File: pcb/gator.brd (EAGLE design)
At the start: 101.6 x 81.3 mm, 89 parts, among them J2 POWER_JACKPTH, X1 USB-A-S, Y1 12MHz

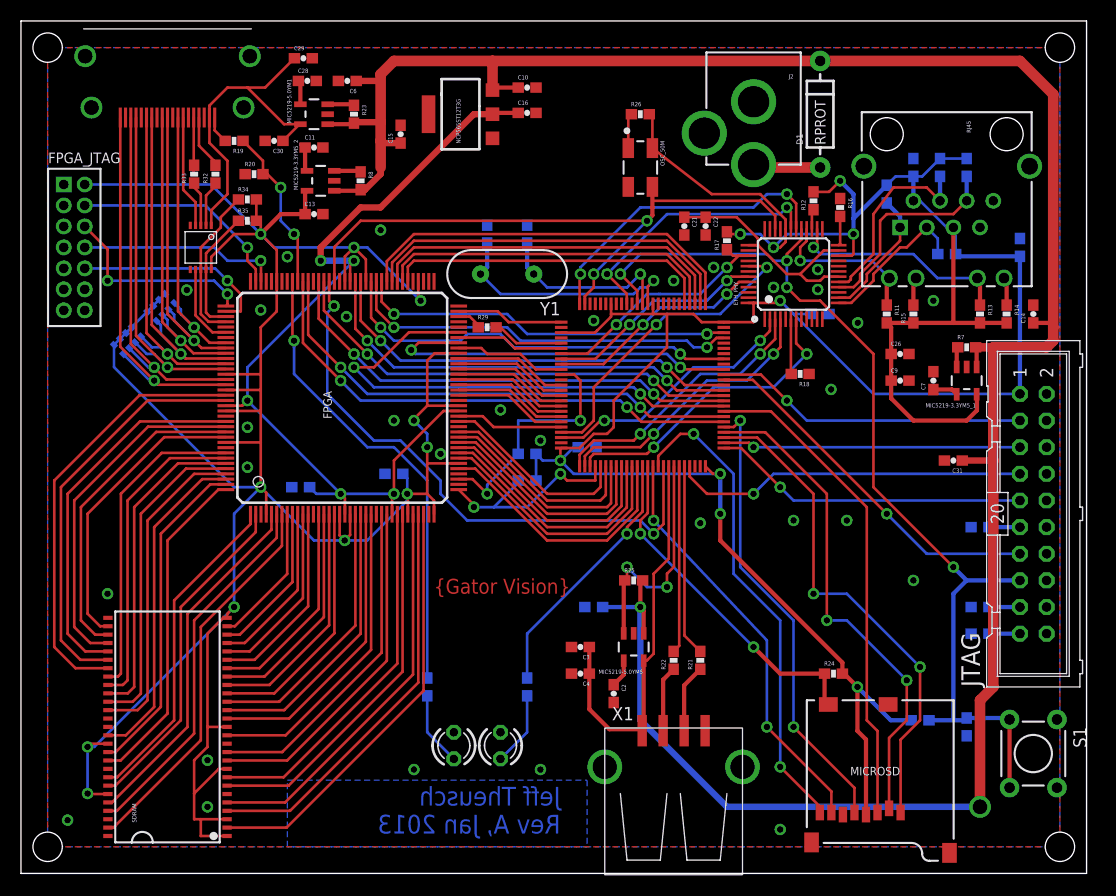
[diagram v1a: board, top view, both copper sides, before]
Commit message: Added tons of decoupling capacitors
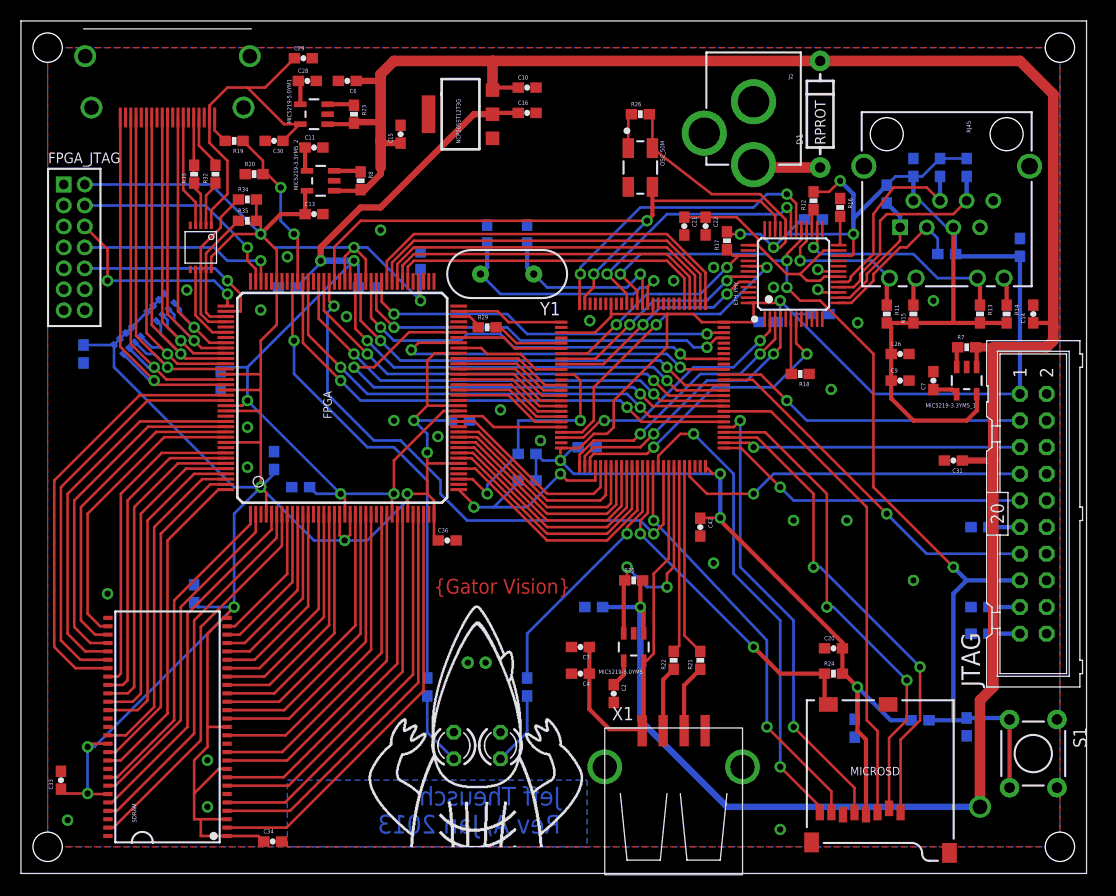
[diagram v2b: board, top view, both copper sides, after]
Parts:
- added C20: 10u, SparkFun-Passives:0603-CAP
- added C23, C32, C33, C34, C35, C36, C37, C38, C39, C40, C41, C42, C43, C44: 100n, SparkFun-Passives:0603-CAP
- added U$4: GATOR_HEAD, gator:GATOR_HEAD
- C13, C16, C30, C4, C9: value 2.2u -> 10u
- moved C12 11.5 mm to (24.1, 39.4), turned to 90 degrees
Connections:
- net +3V3: now also C20.2, C41.1, C42.1, C43.1, C44.1
- net GND: now also C20.1, C23.2, C32.2, C33.2, C34.2, C35.2, C36.2, C37.2, C38.2, C39.2, C40.2, C41.2, C42.2, C43.2, C44.2, U$4.L, U$4.R
- net VCCINT: now also C23.1, C32.1, C40.1
- net VCCIO: now also C33.1, C34.1, C35.1, C36.1, C37.1, C38.1, C39.1
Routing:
- net VCCIO: track 263.3 -> 286.0 mm
- net +3V3: track 272.8 -> 282.3 mm
- net VCCINT: track 86.8 -> 95.8 mm
- net GND: track 0.00 -> 4.17 mm, vias 31 -> 29
- net SD_D2: track 48.0 -> 46.5 mm
- net SD_D3: track 47.2 -> 46.5 mm
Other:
- board outline removed

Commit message: Added Fusion DRC and CAM settings; added SD SCLK pulldown; added large power supply caps
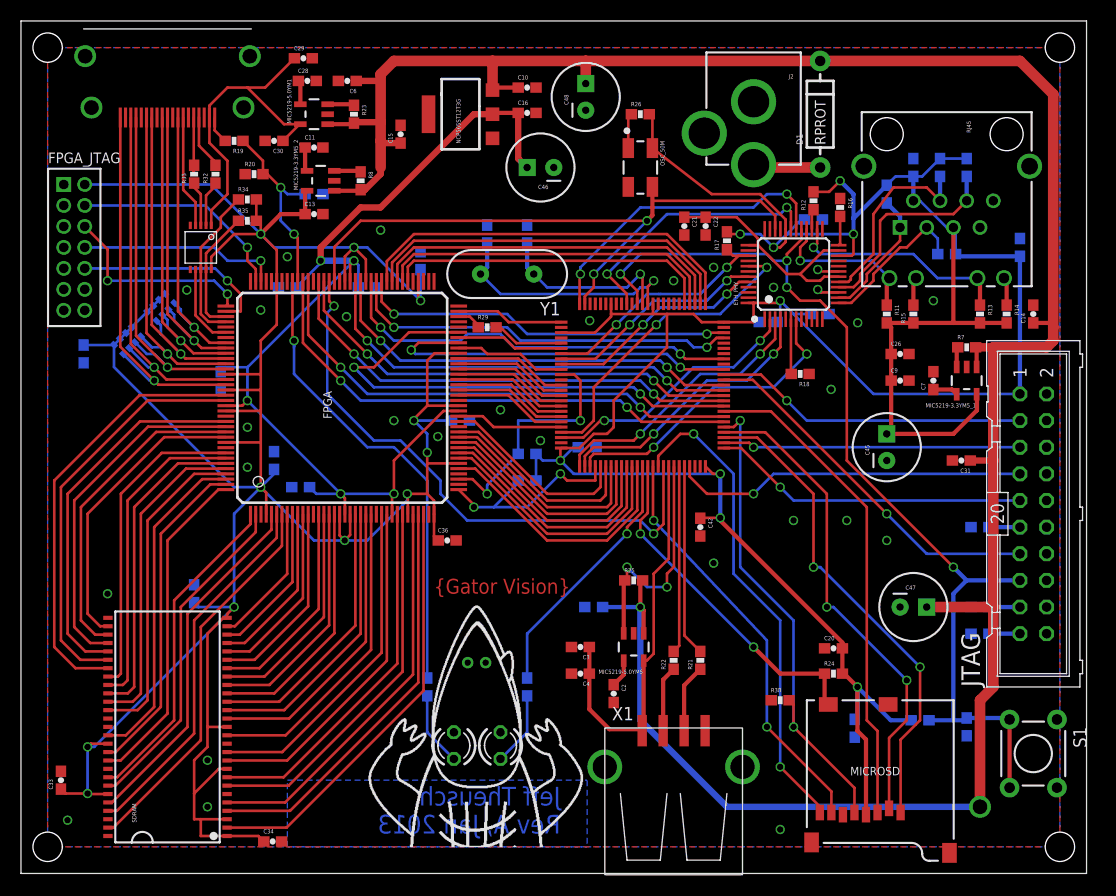
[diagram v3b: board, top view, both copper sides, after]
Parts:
- added C45, C46, C47, C48: 100u, SparkFun-Passives:CPOL-RADIAL-100UF-25V
- added C49: 100n, SparkFun-Passives:0603-CAP
- added R38: 10K, SparkFun-Passives:0603-RES
- C6: value 2.2u -> 10u
- R14, R15: value 110 -> 120
- R19: value 5K6 -> 4K7
- R20: value 10K -> 4K7
- R29: value 50 -> 51
- moved C31 0.76 mm to (89.7, 39.4)
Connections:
- net +3V3: now also C45.1
- net GND: now also C45.2, C46.2, C47.2, C48.2, C49.2, R38.1
- net HDMI_DETECT: now also C49.1
- net SD_CLK: now also R38.2
- net V+: now also C47.1, C48.1
- net VCCINT: now also C46.1
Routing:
- net V+: track 233.9 -> 241.7 mm
- net VCCINT: track 95.8 -> 101.3 mm
- net +3V3: track 282.3 -> 285.9 mm
- net SD_CLK: track 43.7 -> 46.4 mm
- net HDMI_DETECT: track 15.8 -> 18.4 mm

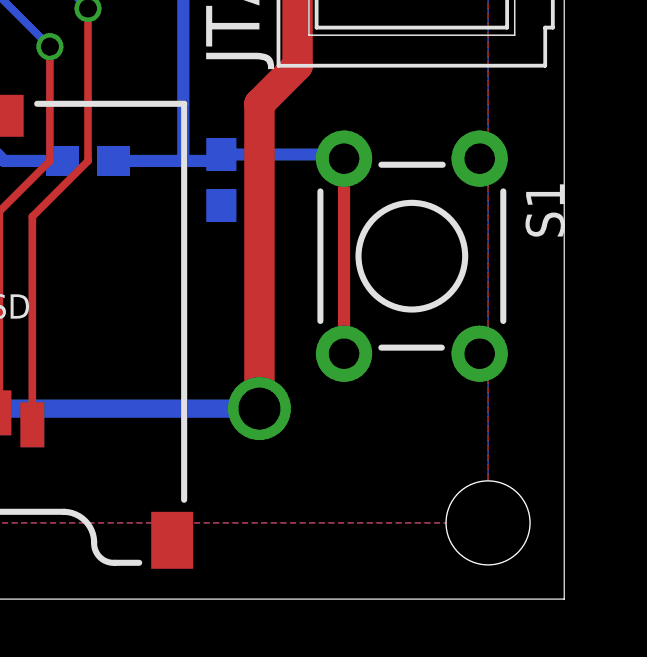
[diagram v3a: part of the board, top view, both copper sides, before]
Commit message: Renamed some parts for clarity
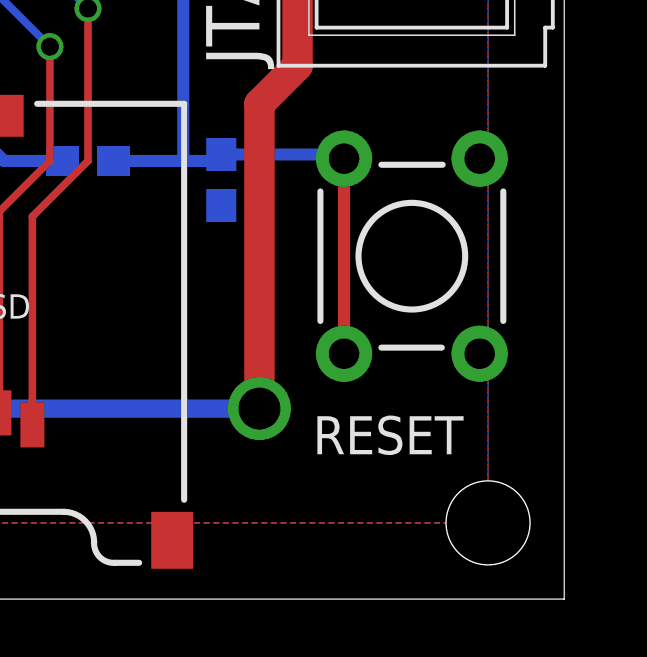
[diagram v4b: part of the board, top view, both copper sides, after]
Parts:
- renumbered S1 to RESET, U$1 to MCU

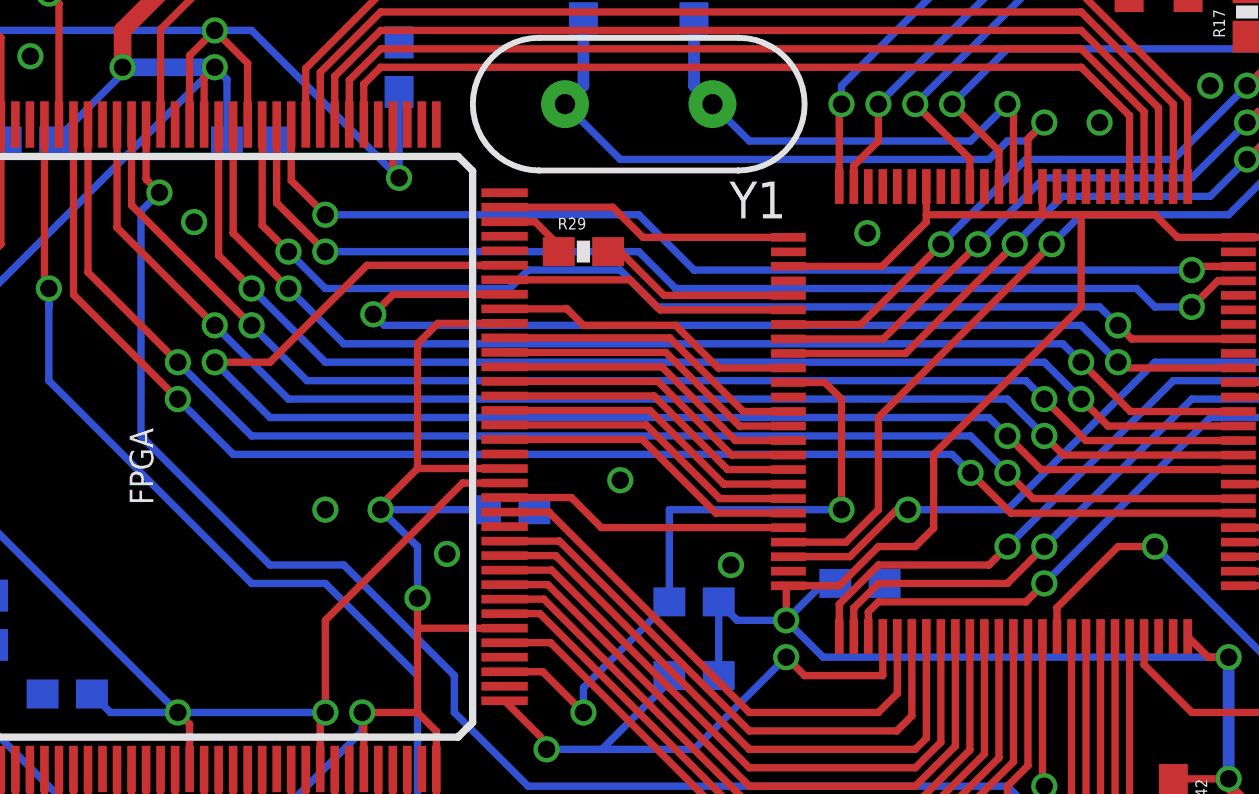
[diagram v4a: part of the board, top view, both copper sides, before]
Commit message: Moved FSMC_CLK to a clock input on the FPGA
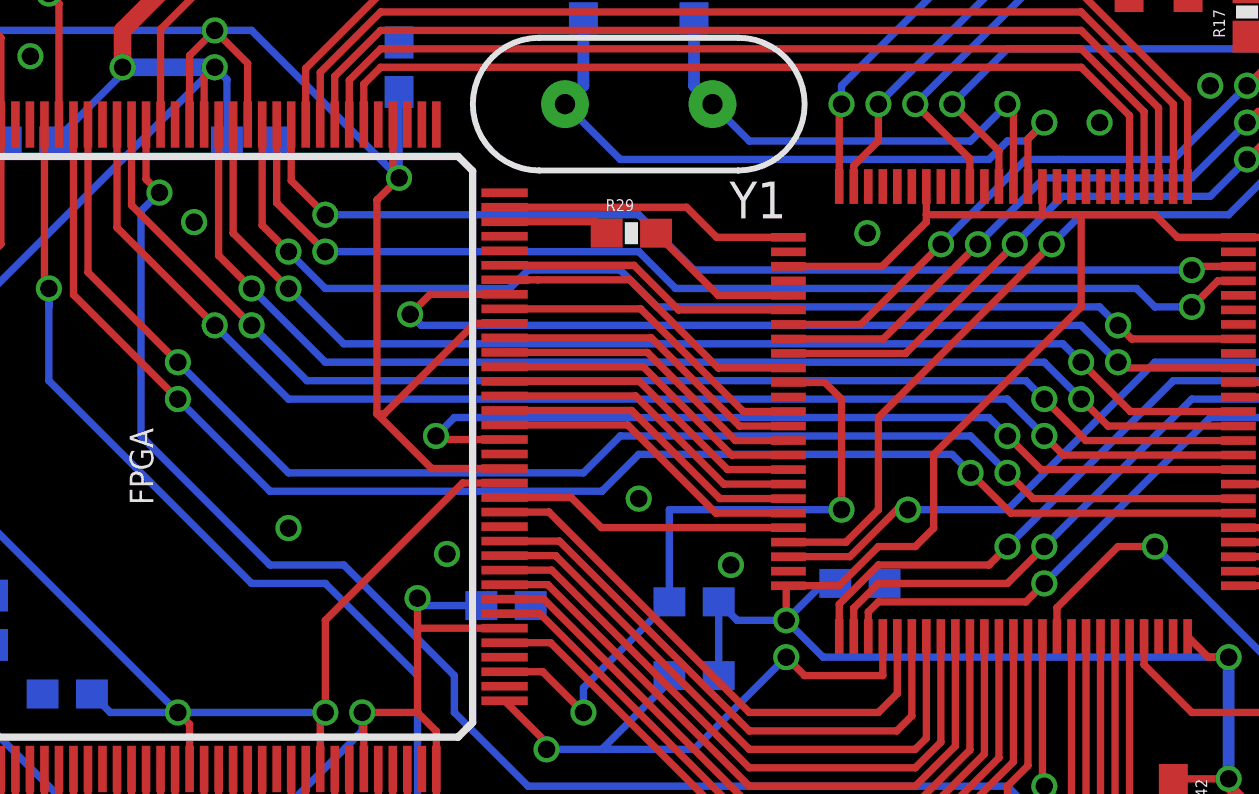
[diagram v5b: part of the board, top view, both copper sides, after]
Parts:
- moved C38 3.30 mm to (41.8, 39.9)
- moved R29 1.77 mm to (46.1, 52.7)
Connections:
- net D10: now also FPGA.P57; no longer FPGA.P56
- net D11: now also FPGA.P56; no longer FPGA.P55
- net D4: now also FPGA.P64; no longer FPGA.P62
- net D5: now also FPGA.P62; no longer FPGA.P61
- net D6: now also FPGA.P61; no longer FPGA.P60
- net D7: now also FPGA.P60; no longer FPGA.P59
- net D8: now also FPGA.P59; no longer FPGA.P58
- net D9: now also FPGA.P58; no longer FPGA.P57
- net FSMC_CLK: now also FPGA.P55; no longer FPGA.P67
- net SPI_MISO: now also FPGA.P67; no longer FPGA.P66
- net VSYNC: now also FPGA.P66; no longer FPGA.P64
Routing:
- net FSMC_CLK: track 48.2 -> 31.1 mm
- net CFG_DIN: track 35.4 -> 32.8 mm
- net VCCIO: track 286.0 -> 287.9 mm, vias 11 -> 10
- net CFG_CLK: track 6.84 -> 5.45 mm
- net N$33: track 2.42 -> 3.68 mm
- net D2: track 49.1 -> 50.2 mm
- net D3: track 47.9 -> 49.0 mm

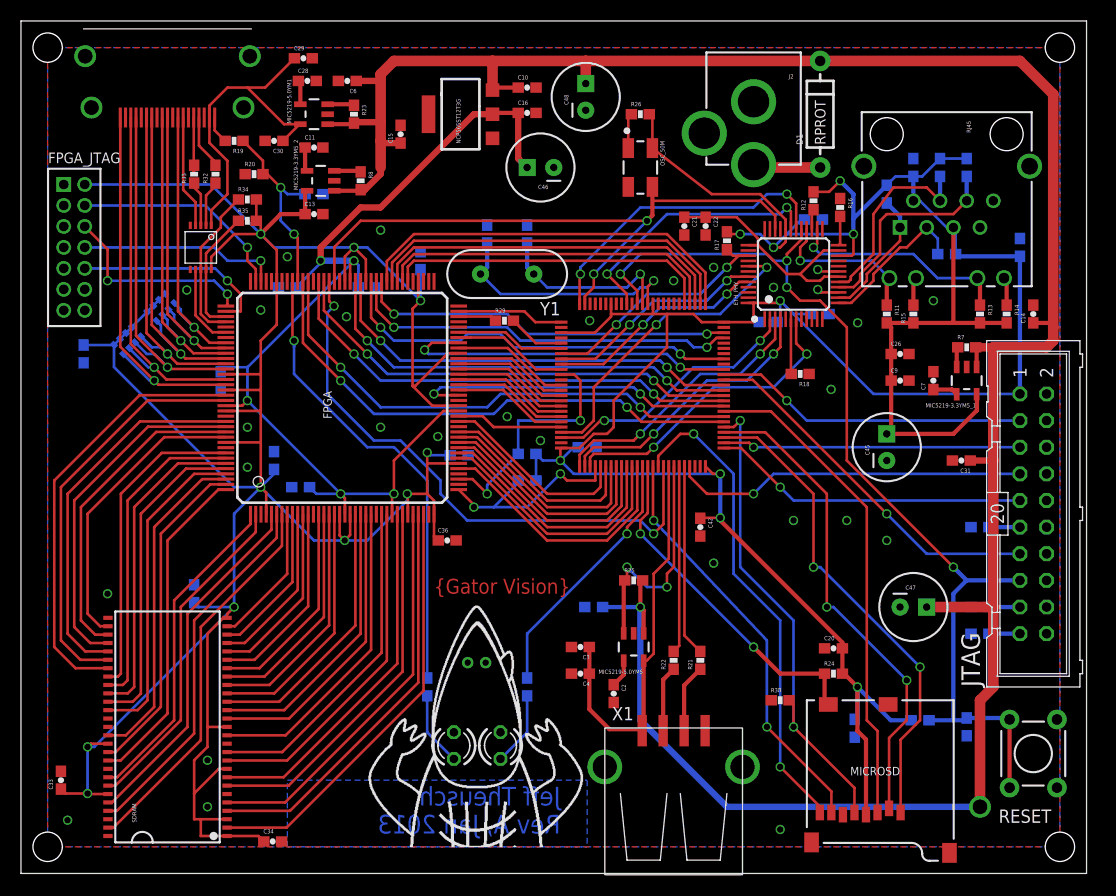
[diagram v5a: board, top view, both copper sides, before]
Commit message: Added pull-ups for sd card and ethernet
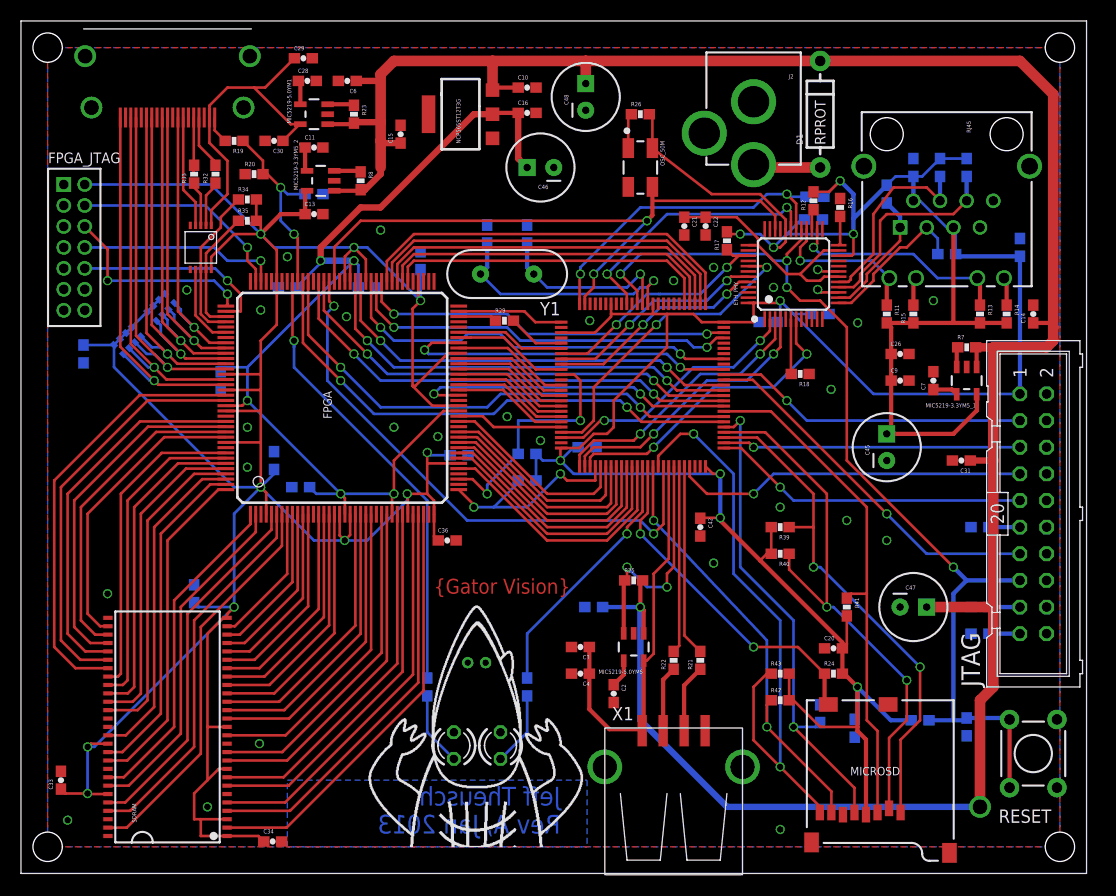
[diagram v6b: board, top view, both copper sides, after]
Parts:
- added R39, R40, R41, R42, R43: 47K, SparkFun-Passives:0603-RES
- added R44: 1K5, SparkFun-Passives:0603-RES
- R26: value 2K2 -> 10K
- R38: value 10K -> 47K
- moved R38 4.02 mm to (76.2, 15.2), flipped to the bottom, turned to 270 degrees
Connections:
- net +3V3: now also R39.2, R40.2, R41.2, R42.2, R43.2, R44.2
- net MII_MDIO: now also R44.1
- net SD_CMD: now also R41.1
- net SD_D0: now also R42.1
- net SD_D1: now also R43.1
- net SD_D2: now also R39.1
- net SD_D3: now also R40.1
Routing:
- net +3V3: track 285.9 -> 305.3 mm
- net SD_D1: track 46.3 -> 57.2 mm
- net SD_D3: track 46.5 -> 53.0 mm
- net SD_D0: track 39.9 -> 42.6 mm
- net SD_D2: track 46.5 -> 48.8 mm
- net SD_CMD: track 47.0 -> 49.0 mm
- net MII_MDIO: track 29.8 -> 31.7 mm
- net VCCIO: track 287.9 -> 286.1 mm
- net FPGA_CLK1: track 55.4 -> 53.9 mm
- net LED_LEFT: track 45.3 -> 43.8 mm
- net SDR_DQ14: track 35.4 -> 36.2 mm
- net SDR_DQ13: track 34.2 -> 34.9 mm
- net SDR_DQ12: track 32.1 -> 32.9 mm
- net SDR_DQ15: track 37.1 -> 37.8 mm
- net HDMI_5V: track 31.6 -> 30.9 mm

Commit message: Added Digikey parts for everything except resistors and capacitors
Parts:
- MIC5219-3.3YM5_1, MIC5219-3.3YM5_2: value V_REG_LDOSMD -> 3.3V
- MIC5219-5.0YM1, MIC5219-5.0YM5: value V_REG_LDOSMD -> 5.0V
